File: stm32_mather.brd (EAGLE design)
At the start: 100 x 80 mm, 50 parts

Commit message: ledとか追加した
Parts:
- added LED2: (no value), user_leds:1608
- added R14, R15: 10k, user_rcl:1608
- added R_I1: (no value), user_rcl:0603X4RESISTOR
- added U$15: RGB_LED, user_leds:RGB_LED
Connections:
- new net B_LED: MCU1.35, R_I1.6
- new net ERROR: MCU1.33, R_I1.8
- new net G_LED: MCU1.34, R_I1.7
- new net N$10: R_I1.1, U$15.R_K
- new net N$29: R_I1.2, U$15.G_K
- new net N$31: R_I1.3, U$15.B_K
- new net N$32: LED2.A, R_I1.4
- net GND: now also LED2.K, U$15.B_A, U$15.G_A, U$15.R_A
- net USART1_RX: now also R14.1
- net USART1_TX: now also R15.1
- net V3.3: now also R14.2, R15.2, R_I1.5
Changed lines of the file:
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@@
 <attribute name="VALUE" x="-5.715" y="-34.925" size="1.27" layer="27"/>
+</element>
+<element name="R14" library="user_rcl" package="1608" value="10k" x="-5.08" y="-38.1" smashed="yes">
+<attribute name="NAME" x="-5.715" y="-37.465" size="1.27" layer="25"/>
+<attribute name="VALUE" x="-5.715" y="-40.005" size="1.27" layer="27"/>
+</element>
+<element name="R15" library="user_rcl" package="1608" value="10k" x="-5.08" y="-43.18" smashed="yes">
+<attribute name="NAME" x="-5.715" y="-42.545" size="1.27" layer="25"/>
+<attribute name="VALUE" x="-5.715" y="-45.085" size="1.27" layer="27"/>
+</element>
+<element name="R_I1" library="user_rcl" package="0603X4RESISTOR" value="" x="-2.54" y="-50.8" smashed="yes">
+<attribute name="NAME" x="-4.5125" y="-49.53" size="1.27" layer="25"/>
+<attribute name="VALUE" x="-4.5125" y="-53.34" size="1.27" layer="27"/>
+</element>
+<element name="U$15" library="user_leds" package="RGB_LED" value="RGB_LED" x="-5.08" y="-55.88" smashed="yes"/>
+<element name="LED2" library="user_leds" package="1608" value="" x="-5.08" y="-63.5" smashed="yes">
+<attribute name="NAME" x="-6.35" y="-62.23" size="0.4064" layer="25"/>
+<attribute name="VALUE" x="-6.35" y="-62.738" size="0.4064" layer="27"/>
 </element>
 </elements>
@@
 <contactref element="U$22" pad="7"/>
 <contactref element="U$22" pad="11"/>
+<contactref element="LED2" pad="K"/>
+<contactref element="U$15" pad="R_A"/>
+<contactref element="U$15" pad="G_A"/>
+<contactref element="U$15" pad="B_A"/>
 <wire x1="79.83" y1="67.94" x2="82.37" y2="67.94" width="0" layer="19" extent="1-1"/>
 <wire x1="62.37" y1="67.94" x2="79.83" y2="67.94" width="0" layer="19" extent="1-1"/>
@@
 <wire x1="-4" y1="-5.715" x2="-4" y2="-4.445" width="0" layer="19" extent="1-1"/>
 <wire x1="-4" y1="-8.255" x2="-4" y2="-5.715" width="0" layer="19" extent="1-1"/>
+<wire x1="-1.58" y1="-55.88" x2="-4" y2="-8.255" width="0" layer="19" extent="1-1"/>
+<wire x1="-1.58" y1="-57.23" x2="-1.58" y2="-55.88" width="0" layer="19" extent="1-1"/>
+<wire x1="-1.58" y1="-58.58" x2="-1.58" y2="-57.23" width="0" layer="19" extent="1-1"/>
+<wire x1="-4.23" y1="-63.5" x2="-1.58" y2="-58.58" width="0" layer="19" extent="1-1"/>
 </signal>
 <signal name="V3.3">
@@
 <contactref element="R11" pad="1"/>
 <contactref element="R12" pad="1"/>
+<contactref element="R14" pad="2"/>
+<contactref element="R15" pad="2"/>
+<contactref element="R_I1" pad="5"/>
 <wire x1="43.18" y1="36.41" x2="48.26" y2="38.95" width="0" layer="19" extent="1-1"/>
 <wire x1="41.1" y1="38.1" x2="43.18" y2="36.41" width="0" layer="19" extent="1-1"/>
@@
 <wire x1="-5.93" y1="-15.24" x2="-4" y2="-3.175" width="0" layer="19" extent="1-1"/>
 <wire x1="-5.93" y1="-20.32" x2="-5.93" y2="-15.24" width="0" layer="19" extent="1-1"/>
+<wire x1="-4.23" y1="-38.1" x2="-5.93" y2="-20.32" width="0" layer="19" extent="1-1"/>
+<wire x1="-4.23" y1="-43.18" x2="-4.23" y2="-38.1" width="0" layer="19" extent="1-1"/>
+<wire x1="-1.265" y1="-49.95" x2="-4.23" y2="-43.18" width="0" layer="19" extent="1-1"/>
 </signal>
 <signal name="N$3">
@@
 <contactref element="MCU1" pad="58"/>
 <contactref element="U$14" pad="6"/>
+<contactref element="R15" pad="1"/>
 <wire x1="19.13" y1="19.43" x2="80.33" y2="36.86" width="0" layer="19" extent="1-1"/>
+<wire x1="-5.93" y1="-43.18" x2="19.13" y2="19.43" width="0" layer="19" extent="1-1"/>
 </signal>
 <signal name="USART1_RX">
 <contactref element="MCU1" pad="59"/>
 <contactref element="U$14" pad="4"/>
+<contactref element="R14" pad="1"/>
 <wire x1="18.63" y1="19.43" x2="82.23" y2="36.86" width="0" layer="19" extent="1-1"/>
+<wire x1="-5.93" y1="-38.1" x2="18.63" y2="19.43" width="0" layer="19" extent="1-1"/>
 </signal>
 <signal name="V3.3_AR">
@@
 <wire x1="-1.27" y1="-27.94" x2="-4.23" y2="-33.02" width="0" layer="19" extent="1-1"/>
 </signal>
+<signal name="N$10">
+<contactref element="U$15" pad="R_K"/>
+<contactref element="R_I1" pad="1"/>
+<wire x1="-3.815" y1="-51.65" x2="-5.08" y2="-55.88" width="0" layer="19" extent="1-1"/>
+</signal>
+<signal name="N$29">
+<contactref element="U$15" pad="G_K"/>
+<contactref element="R_I1" pad="2"/>
+<wire x1="-2.94" y1="-51.65" x2="-5.08" y2="-57.23" width="0" layer="19" extent="1-1"/>
+</signal>
+<signal name="N$31">
+<contactref element="U$15" pad="B_K"/>
+<contactref element="R_I1" pad="3"/>
+<wire x1="-2.14" y1="-51.65" x2="-5.08" y2="-58.58" width="0" layer="19" extent="1-1"/>
+</signal>
+<signal name="N$32">
+<contactref element="LED2" pad="A"/>
+<contactref element="R_I1" pad="4"/>
+<wire x1="-1.265" y1="-51.65" x2="-5.93" y2="-63.5" width="0" layer="19" extent="1-1"/>
+</signal>
+<signal name="B_LED">
+<contactref element="R_I1" pad="6"/>
+<contactref element="MCU1" pad="35"/>
+<wire x1="25.53" y1="11.03" x2="-2.14" y2="-49.95" width="0" layer="19" extent="1-1"/>
+</signal>
+<signal name="G_LED">
+<contactref element="R_I1" pad="7"/>
+<contactref element="MCU1" pad="34"/>
+<wire x1="25.53" y1="10.53" x2="-2.94" y2="-49.95" width="0" layer="19" extent="1-1"/>
+</signal>
+<signal name="ERROR">
+<contactref element="R_I1" pad="8"/>
+<contactref element="MCU1" pad="33"/>
+<wire x1="25.53" y1="10.03" x2="-3.815" y2="-49.95" width="0" layer="19" extent="1-1"/>
+</signal>
 </signals>

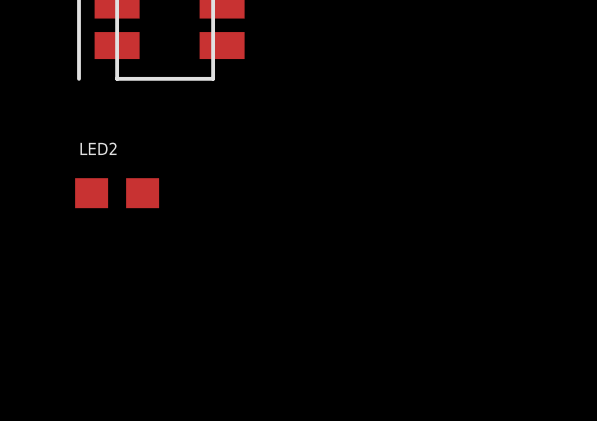
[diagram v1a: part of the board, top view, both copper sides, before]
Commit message: bootピンの設定をした
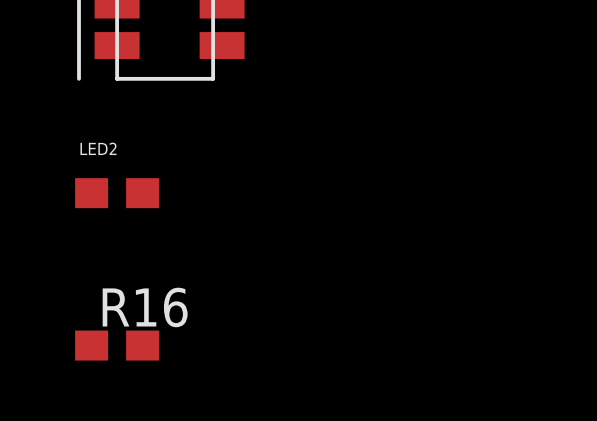
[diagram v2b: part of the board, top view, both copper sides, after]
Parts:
- added R16: 10k, user_rcl:1608
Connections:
- new net N$33: MCU1.60, R16.1
- net GND: now also R16.2
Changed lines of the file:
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@@
 <attribute name="VALUE" x="-6.35" y="-62.738" size="0.4064" layer="27"/>
+</element>
+<element name="R16" library="user_rcl" package="1608" value="10k" x="-5.08" y="-68.58" smashed="yes">
+<attribute name="NAME" x="-5.715" y="-67.945" size="1.27" layer="25"/>
+<attribute name="VALUE" x="-5.715" y="-70.485" size="1.27" layer="27"/>
 </element>
 </elements>
@@
 <contactref element="U$15" pad="G_A"/>
 <contactref element="U$15" pad="B_A"/>
+<contactref element="R16" pad="2"/>
 <wire x1="79.83" y1="67.94" x2="82.37" y2="67.94" width="0" layer="19" extent="1-1"/>
 <wire x1="62.37" y1="67.94" x2="79.83" y2="67.94" width="0" layer="19" extent="1-1"/>
@@
 <wire x1="-1.58" y1="-58.58" x2="-1.58" y2="-57.23" width="0" layer="19" extent="1-1"/>
 <wire x1="-4.23" y1="-63.5" x2="-1.58" y2="-58.58" width="0" layer="19" extent="1-1"/>
+<wire x1="-4.23" y1="-68.58" x2="-4.23" y2="-63.5" width="0" layer="19" extent="1-1"/>
 </signal>
 <signal name="V3.3">
@@
 <wire x1="25.53" y1="10.03" x2="-3.815" y2="-49.95" width="0" layer="19" extent="1-1"/>
 </signal>
+<signal name="N$33">
+<contactref element="R16" pad="1"/>
+<contactref element="MCU1" pad="60"/>
+<wire x1="18.13" y1="19.43" x2="-5.93" y2="-68.58" width="0" layer="19" extent="1-1"/>
+</signal>
 </signals>
